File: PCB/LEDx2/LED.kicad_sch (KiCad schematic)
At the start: 31 parts, among them J1 Reset, J2 Wago, J3 TC2030-USB-NL-DS, J4 Wago, J5 USB-C-Socket-H, J6 Wago, J7 Wago, U2 ESP32-S3-MINI-1, U5 MD8942

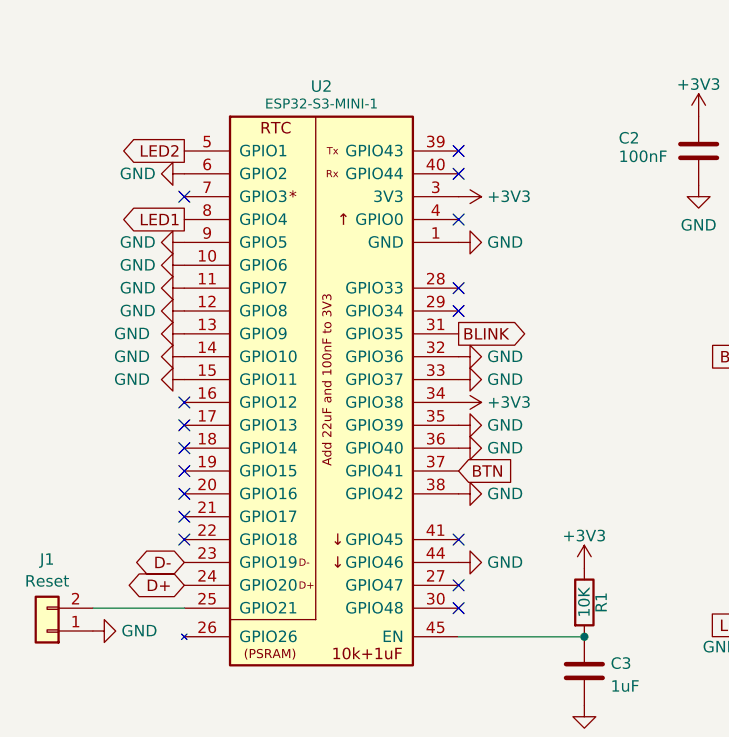
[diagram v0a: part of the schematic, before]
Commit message: Clean up GND GPIOs
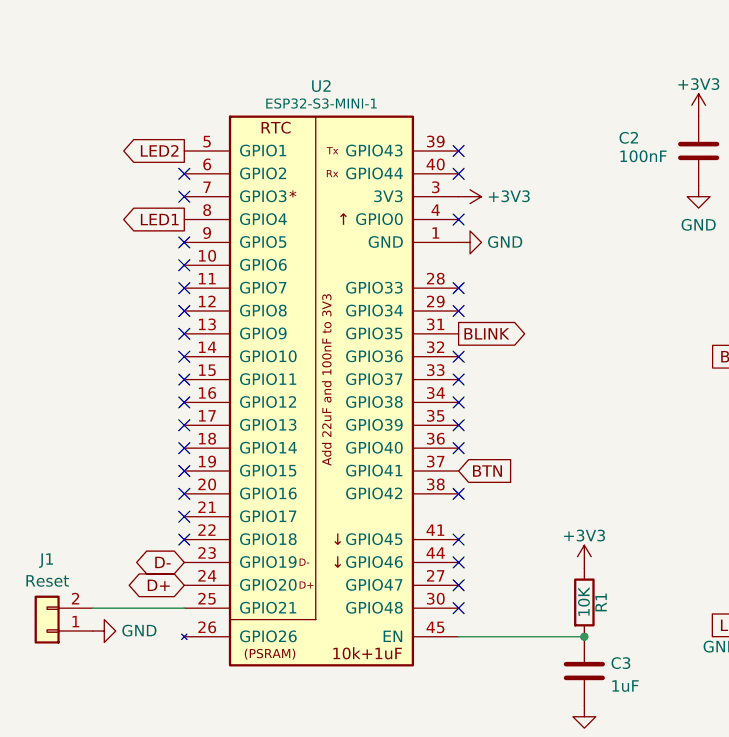
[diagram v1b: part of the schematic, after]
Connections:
- net +3V3: no longer U2.34 (GPIO38)
- net GND: no longer U2.10 (GPIO6), U2.11 (GPIO7), U2.12 (GPIO8), U2.13 (GPIO9), U2.14 (GPIO10), U2.15 (GPIO11), U2.32 (GPIO36), U2.33 (GPIO37), U2.35 (GPIO39), U2.36 (GPIO40), U2.38 (GPIO42), U2.44 (GPIO46), U2.6 (GPIO2), U2.9 (GPIO5)
- no-connect marks 18 -> 33

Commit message: BOM fix
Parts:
- C6: value 10uF 50V -> 10uF 35V; LCSC Part # C1591 -> C194427
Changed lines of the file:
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@@
 			)
 		)
-		(property "Value" "10uF 50V"
+		(property "Value" "10uF 35V"
 			(at 194.945 114.935 0)
 			(effects
@@
 			)
 		)
-		(property "LCSC Part #" "C1591"
+		(property "LCSC Part #" "C194427"
 			(at 188.595 114.935 0)
 			(effects

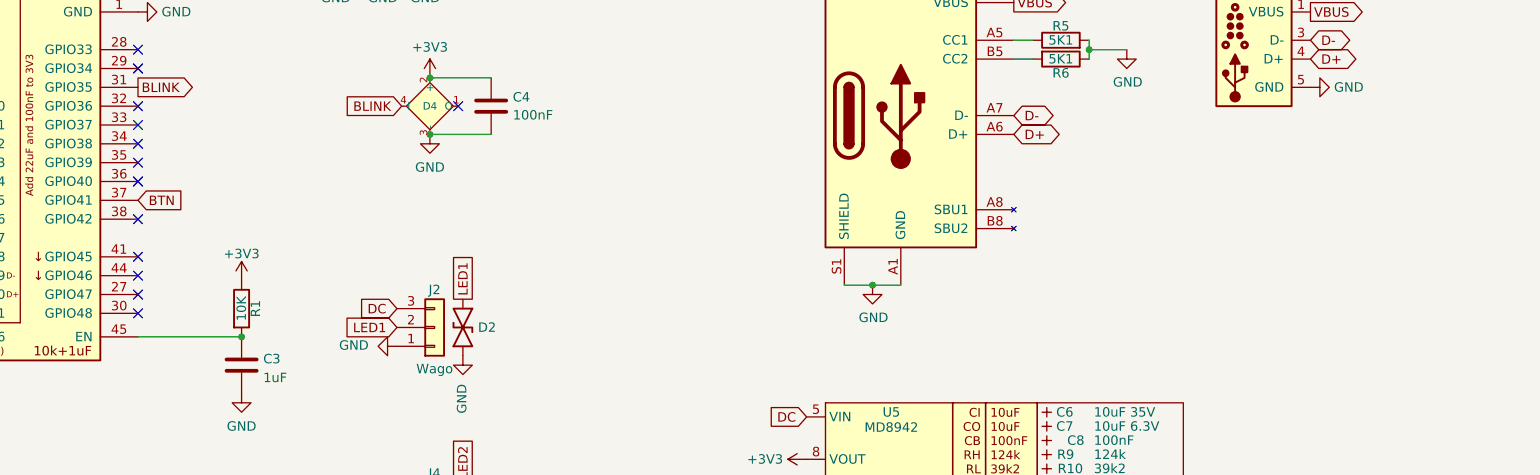
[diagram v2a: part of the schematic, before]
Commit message: Mic on 2 LED module
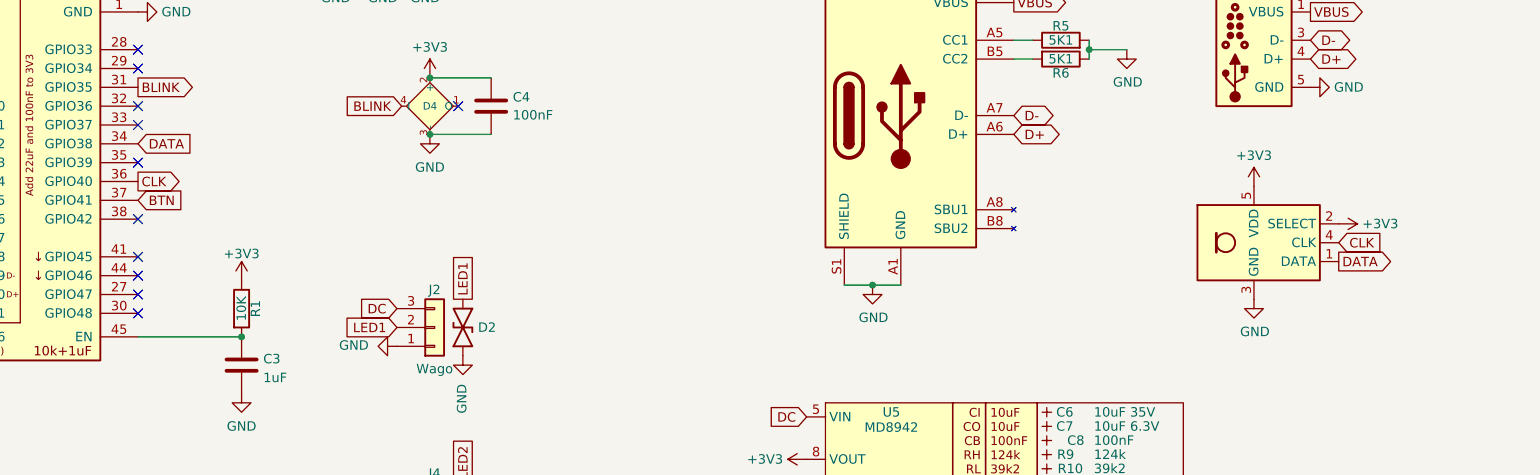
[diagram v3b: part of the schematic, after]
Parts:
- added T1: T3902_MEMS_Mic, RevK:T3902_MEMS_Mic, symbol RevK:T3902_MEMS_Mic
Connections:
- net +3V3: now also T1.2 (SELECT), T1.5 (VDD)
- net GND: now also T1.3 (GND)
- net DATA: now reaches U2.34 (GPIO38)
- net DATA: now also T1.1 (DATA)
- net CLK: now reaches U2.36 (GPIO40)
- net CLK: now also T1.4 (CLK)
- no-connect marks 33 -> 31

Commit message: Library update
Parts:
- renumbered C6 to C10, C7 to C11, C8 to C12, C3 to C9, D4 to D1, R10 to R14, R11 to R15, R1 to R2, R9 to R4, U2 to U6, U5 to U7
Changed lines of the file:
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@@
 (kicad_sch
-	(version 20231120)
+	(version 20241209)
 	(generator "eeschema")
-	(generator_version "8.0")
+	(generator_version "9.0")
 	(paper "A4")
 	(title_block
@@
 		(on_board yes)
 		(dnp no)
-		(property "Reference" "C6"
+		(property "Reference" "C10"
 			(at 189.865 114.935 0)
 			(effects
@@
 		(on_board yes)
 		(dnp no)
-		(property "Reference" "C8"
+		(property "Reference" "C12"
 			(at 193.675 118.745 90)
 			(effects
@@
 		(on_board yes)
 		(dnp no)
-		(property "Reference" "R11"
+		(property "Reference" "R15"
 			(at 189.865 124.46 0)
 			(effects
@@
 		(dnp no)
 		(fields_autoplaced yes)
-		(property "Reference" "#PWR0105"
+		(property "Reference" "#PWR022"
 			(at 80.01 118.745 0)
 			(effects
@@
 		(on_board yes)
 		(dnp no)
-		(property "Reference" "R9"
+		(property "Reference" "R4"
 			(at 191.135 120.65 0)
 			(effects
@@
 		(dnp no)
 		(fields_autoplaced yes)
-		(property "Reference" "U2"
+		(property "Reference" "U6"
 			(at 50.8 43.6332 0)
 			(effects
@@
 		(dnp no)
 		(fields_autoplaced yes)
-		(property "Reference" "#PWR03"
+		(property "Reference" "#PWR019"
 			(at 62.23 55.88 0)
 			(effects
@@
 		(on_board yes)
 		(dnp no)
-		(property "Reference" "#PWR010"
+		(property "Reference" "#PWR025"
 			(at 167.64 137.16 0)
 			(effects
@@
 		(dnp no)
 		(fields_autoplaced yes)
-		(property "Reference" "#PWR0106"
+		(property "Reference" "#PWR021"
 			(at 80.01 100.965 0)
 			(effects
@@
 		(dnp no)
 		(fields_autoplaced yes)
-		(property "Reference" "#PWR01"
+		(property "Reference" "#PWR020"
 			(at 72.39 60.96 0)
 			(effects
@@
 		(on_board yes)
 		(dnp no)
-		(property "Reference" "D4"
+		(property "Reference" "D1"
 			(at 105.41 73.66 0)
 			(do_not_autoplace yes)
@@
 		(on_board yes)
 		(dnp no)
-		(property "Reference" "R1"
+		(property "Reference" "R2"
 			(at 81.915 100.965 90)
 			(effects
@@
 		(dnp no)
 		(fields_autoplaced yes)
-		(property "Reference" "#PWR019"
+		(property "Reference" "#PWR09"
 			(at 105.41 83.82 0)
 			(effects
@@
 		(on_board yes)
 		(dnp no)
-		(property "Reference" "U5"
+		(property "Reference" "U7"
 			(at 167.64 114.935 0)
 			(effects
@@
 		(on_board yes)
 		(dnp no)
-		(property "Reference" "C7"
+		(property "Reference" "C11"
 			(at 189.865 116.84 0)
 			(effects
@@
 		(dnp no)
 		(fields_autoplaced yes)
-		(property "Reference" "#PWR09"
+		(property "Reference" "#PWR024"
 			(at 160.02 121.285 0)
 			(effects
@@
 		(dnp no)
 		(fields_autoplaced yes)
-		(property "Reference" "C3"
+		(property "Reference" "C9"
 			(at 82.931 107.7503 0)
 			(effects
@@
 		(on_board yes)
 		(dnp no)
-		(property "Reference" "R10"
+		(property "Reference" "R14"
 			(at 191.77 122.555 90)
 			(effects
@@
 		)
 	)
+	(embedded_fonts no)
 )

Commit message: PCB Update
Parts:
- C1: JLCPCB Rotation Offset 180 -> (none); LCSC Part # C122649 -> (none); MPN (none) -> C122649
- C10: LCSC Part # C194427 -> (none); MPN (none) -> C194427
- C11: LCSC Part # C1691 -> (none); MPN (none) -> C1691
- D1: LCSC Part # C5349953 -> (none); MPN (none) -> C5349953
- D2, D3, D4: LCSC Part # C5137770 -> (none); MPN (none) -> C5137770
- J2, J4: LCSC Part # C2765056 -> (none); MPN (none) -> C2765056
- J5: LCSC Part # C709357 -> (none); MPN (none) -> C709357
- J6, J7: LCSC Part # C2765055 -> (none); MPN (none) -> C2765055
- T1: LCSC Part # C3171752 -> (none); MPN (none) -> C3171752
- U6: LCSC Part # C3013941 -> (none); MPN (none) -> C3013941
- U7: LCSC Part # C2684786 -> (none); MPN (none) -> C2684786
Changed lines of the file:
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@@
 			)
 		)
-		(property "LCSC Part #" "C194427"
+		(property "MPN" "C194427"
 			(at 188.595 114.935 0)
 			(effects
@@
 			)
 		)
-		(property "LCSC Part #" "C2765055"
+		(property "MPN" "C2765055"
 			(at 106.045 153.67 0)
 			(effects
@@
 			)
 		)
-		(property "LCSC Part #" "C2765056"
+		(property "MPN" "C2765056"
 			(at 106.045 103.505 0)
 			(effects
@@
 			)
 		)
-		(property "LCSC Part #" "C2765055"
+		(property "MPN" "C2765055"
 			(at 106.045 176.53 0)
 			(effects
@@
 			)
 		)
-		(property "LCSC Part #" "C3013941"
+		(property "MPN" "C3013941"
 			(at 50.8 109.855 0)
 			(effects
@@
 			)
 		)
-		(property "LCSC Part #" "C2765056"
+		(property "MPN" "C2765056"
 			(at 106.045 128.27 0)
 			(effects
@@
 			)
 		)
-		(property "LCSC Part #" "C5137770"
+		(property "MPN" "C5137770"
 			(at 106.68 128.27 0)
 			(effects
@@
 			)
 		)
-		(property "LCSC Part #" "C3171752"
+		(property "MPN" "C3171752"
 			(at 216.535 92.075 0)
 			(effects
@@
 			)
 		)
-		(property "LCSC Part #" "C709357"
+		(property "MPN" "C709357"
 			(at 168.91 74.93 0)
 			(effects
@@
 			)
 		)
-		(property "LCSC Part #" "C122649"
-			(at 104.775 50.8 0)
-			(effects
-				(font
-					(size 1.27 1.27)
-				)
-				(hide yes)
-			)
-		)
-		(property "JLCPCB Rotation Offset" "180"
+		(property "MPN" "C122649"
 			(at 104.775 50.8 0)
 			(effects
@@
 			)
 		)
-		(property "LCSC Part #" "C5349953"
+		(property "MPN" "C5349953"
 			(at 106.68 62.23 0)
 			(effects
@@
 			)
 		)
-		(property "LCSC Part #" "C2684786"
+		(property "MPN" "C2684786"
 			(at 167.64 147.955 0)
 			(effects
@@
 			)
 		)
-		(property "LCSC Part #" "C5137770"
+		(property "MPN" "C5137770"
 			(at 106.68 152.4 0)
 			(effects
@@
 			)
 		)
-		(property "LCSC Part #" "C1691"
+		(property "MPN" "C1691"
 			(at 188.595 116.84 0)
 			(effects
@@
 			)
 		)
-		(property "LCSC Part #" "C5137770"
+		(property "MPN" "C5137770"
 			(at 106.68 103.505 0)
 			(effects
